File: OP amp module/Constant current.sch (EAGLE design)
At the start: 6 parts, among them IC1 LM358N

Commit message: Constant current
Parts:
- removed R3: 1M, rcl:R-US_0414/15
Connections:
- removed net N$1: IC1A.+IN, IC2.OUT, R1.1
- removed net N$5: IC1A.-IN, R2.2, VR1.E, VR1.S
- new net N$2: IC1A.OUT, IC2.ADJ, VR1.A, VR1.S
- new net N$4: IC2.OUT, R1.1, R2.2
- net GND: no longer R3.2
- net N$3: now also IC1A.-IN, R2.1, VR1.E; no longer IC1A.OUT, IC2.ADJ, VR1.A
- net N$6: now also IC1A.+IN; no longer R2.1, R3.1
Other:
- moved on the sheet: IC1A, R1, R2, VR1
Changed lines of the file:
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@@
 <part name="VR1" library="My Library" deviceset="POT" device="100K_3362U" value="5k"/>
 <part name="R2" library="rcl" deviceset="R-US_" device="0414/15" value="1k"/>
-<part name="R3" library="rcl" deviceset="R-US_" device="0414/15" value="1M"/>
 </parts>
 <sheets>
@@
 </plain>
 <instances>
-<instance part="IC1" gate="A" x="40.64" y="55.88" rot="MR0"/>
+<instance part="IC1" gate="A" x="35.56" y="45.72" rot="R180"/>
 <instance part="IC2" gate="1" x="27.94" y="73.66"/>
-<instance part="R1" gate="G$1" x="58.42" y="73.66"/>
+<instance part="R1" gate="G$1" x="63.5" y="63.5" rot="R270"/>
 <instance part="P+1" gate="1" x="12.7" y="78.74"/>
-<instance part="IC1" gate="P" x="40.64" y="55.88"/>
-<instance part="P+2" gate="1" x="40.64" y="66.04"/>
-<instance part="GND1" gate="1" x="40.64" y="30.48"/>
-<instance part="GND2" gate="1" x="71.12" y="30.48"/>
-<instance part="GND3" gate="1" x="12.7" y="30.48"/>
-<instance part="VR1" gate="G$1" x="48.26" y="45.72" rot="R270"/>
-<instance part="R2" gate="G$1" x="60.96" y="53.34" rot="R180"/>
-<instance part="R3" gate="G$1" x="66.04" y="43.18" rot="R270"/>
+<instance part="IC1" gate="P" x="35.56" y="45.72"/>
+<instance part="P+2" gate="1" x="35.56" y="55.88"/>
+<instance part="GND1" gate="1" x="35.56" y="27.94"/>
+<instance part="GND2" gate="1" x="63.5" y="27.94"/>
+<instance part="GND3" gate="1" x="7.62" y="27.94"/>
+<instance part="VR1" gate="G$1" x="45.72" y="63.5" rot="R270"/>
+<instance part="R2" gate="G$1" x="53.34" y="68.58" rot="R90"/>
 </instances>
 <busses>
 </busses>
 <nets>
-<net name="N$1" class="0">
-<segment>
-<pinref part="IC2" gate="1" pin="OUT"/>
-<pinref part="R1" gate="G$1" pin="1"/>
-<wire x1="38.1" y1="73.66" x2="53.34" y2="73.66" width="0.1524" layer="91"/>
-<wire x1="53.34" y1="73.66" x2="53.34" y2="58.42" width="0.1524" layer="91"/>
-<pinref part="IC1" gate="A" pin="+IN"/>
-<wire x1="53.34" y1="58.42" x2="48.26" y2="58.42" width="0.1524" layer="91"/>
-<junction x="53.34" y="73.66"/>
-</segment>
-</net>
-<net name="N$3" class="0">
-<segment>
-<pinref part="IC2" gate="1" pin="ADJ"/>
-<wire x1="27.94" y1="66.04" x2="27.94" y2="55.88" width="0.1524" layer="91"/>
-<pinref part="IC1" gate="A" pin="OUT"/>
-<wire x1="27.94" y1="55.88" x2="33.02" y2="55.88" width="0.1524" layer="91"/>
-<wire x1="43.18" y1="45.72" x2="27.94" y2="45.72" width="0.1524" layer="91"/>
-<wire x1="27.94" y1="45.72" x2="27.94" y2="55.88" width="0.1524" layer="91"/>
-<junction x="27.94" y="55.88"/>
-<pinref part="VR1" gate="G$1" pin="A"/>
-</segment>
-</net>
 <net name="VCC" class="0">
 <segment>
@@
 <pinref part="P+2" gate="1" pin="VCC"/>
 <pinref part="IC1" gate="P" pin="V+"/>
-<wire x1="40.64" y1="66.04" x2="40.64" y2="63.5" width="0.1524" layer="91"/>
+<wire x1="35.56" y1="55.88" x2="35.56" y2="53.34" width="0.1524" layer="91"/>
 </segment>
 </net>
@@
 <pinref part="IC1" gate="P" pin="V-"/>
 <pinref part="GND1" gate="1" pin="GND"/>
-<wire x1="40.64" y1="48.26" x2="40.64" y2="33.02" width="0.1524" layer="91"/>
+<wire x1="35.56" y1="38.1" x2="35.56" y2="30.48" width="0.1524" layer="91"/>
 </segment>
 <segment>
-<wire x1="81.28" y1="35.56" x2="71.12" y2="35.56" width="0.1524" layer="91"/>
+<wire x1="68.58" y1="33.02" x2="63.5" y2="33.02" width="0.1524" layer="91"/>
 <pinref part="GND2" gate="1" pin="GND"/>
-<wire x1="71.12" y1="35.56" x2="71.12" y2="33.02" width="0.1524" layer="91"/>
-<pinref part="R3" gate="G$1" pin="2"/>
-<wire x1="71.12" y1="35.56" x2="66.04" y2="35.56" width="0.1524" layer="91"/>
-<wire x1="66.04" y1="35.56" x2="66.04" y2="38.1" width="0.1524" layer="91"/>
+<wire x1="63.5" y1="33.02" x2="63.5" y2="30.48" width="0.1524" layer="91"/>
 </segment>
 <segment>
 <pinref part="GND3" gate="1" pin="GND"/>
-<wire x1="12.7" y1="33.02" x2="12.7" y2="45.72" width="0.1524" layer="91"/>
-<wire x1="12.7" y1="45.72" x2="5.08" y2="45.72" width="0.1524" layer="91"/>
+<wire x1="7.62" y1="30.48" x2="7.62" y2="40.64" width="0.1524" layer="91"/>
+<wire x1="7.62" y1="40.64" x2="5.08" y2="40.64" width="0.1524" layer="91"/>
 </segment>
 </net>
 <net name="N$6" class="0">
 <segment>
-<pinref part="R2" gate="G$1" pin="1"/>
 <pinref part="R1" gate="G$1" pin="2"/>
-<wire x1="63.5" y1="73.66" x2="66.04" y2="73.66" width="0.1524" layer="91"/>
-<wire x1="66.04" y1="73.66" x2="81.28" y2="73.66" width="0.1524" layer="91"/>
-<wire x1="66.04" y1="53.34" x2="66.04" y2="73.66" width="0.1524" layer="91"/>
-<junction x="66.04" y="73.66"/>
-<pinref part="R3" gate="G$1" pin="1"/>
-<wire x1="66.04" y1="48.26" x2="66.04" y2="53.34" width="0.1524" layer="91"/>
-<junction x="66.04" y="53.34"/>
+<wire x1="63.5" y1="58.42" x2="63.5" y2="43.18" width="0.1524" layer="91"/>
+<pinref part="IC1" gate="A" pin="+IN"/>
+<wire x1="63.5" y1="43.18" x2="68.58" y2="43.18" width="0.1524" layer="91"/>
+<wire x1="43.18" y1="43.18" x2="63.5" y2="43.18" width="0.1524" layer="91"/>
+<junction x="63.5" y="43.18"/>
 </segment>
 </net>
-<net name="N$5" class="0">
+<net name="N$2" class="0">
 <segment>
-<wire x1="55.88" y1="45.72" x2="53.34" y2="45.72" width="0.1524" layer="91"/>
-<pinref part="IC1" gate="A" pin="-IN"/>
-<pinref part="R2" gate="G$1" pin="2"/>
-<wire x1="48.26" y1="53.34" x2="55.88" y2="53.34" width="0.1524" layer="91"/>
-<wire x1="55.88" y1="45.72" x2="55.88" y2="53.34" width="0.1524" layer="91"/>
-<junction x="55.88" y="53.34"/>
+<pinref part="IC1" gate="A" pin="OUT"/>
+<wire x1="27.94" y1="45.72" x2="27.94" y2="63.5" width="0.1524" layer="91"/>
+<pinref part="VR1" gate="G$1" pin="A"/>
+<wire x1="27.94" y1="63.5" x2="40.64" y2="63.5" width="0.1524" layer="91"/>
+<pinref part="IC2" gate="1" pin="ADJ"/>
+<wire x1="27.94" y1="66.04" x2="27.94" y2="63.5" width="0.1524" layer="91"/>
+<wire x1="27.94" y1="63.5" x2="27.94" y2="58.42" width="0.1524" layer="91"/>
+<wire x1="27.94" y1="58.42" x2="27.94" y2="63.5" width="0.1524" layer="91"/>
 <pinref part="VR1" gate="G$1" pin="S"/>
-<wire x1="48.26" y1="40.64" x2="53.34" y2="40.64" width="0.1524" layer="91"/>
-<wire x1="53.34" y1="40.64" x2="53.34" y2="45.72" width="0.1524" layer="91"/>
-<pinref part="VR1" gate="G$1" pin="E"/>
-<junction x="53.34" y="45.72"/>
+<wire x1="45.72" y1="58.42" x2="40.64" y2="58.42" width="0.1524" layer="91"/>
+<wire x1="40.64" y1="58.42" x2="40.64" y2="63.5" width="0.1524" layer="91"/>
+<junction x="27.94" y="63.5"/>
+<junction x="40.64" y="63.5"/>
 </segment>
 </net>
+<net name="N$3" class="0">
+<segment>
+<pinref part="VR1" gate="G$1" pin="E"/>
+<pinref part="R2" gate="G$1" pin="1"/>
+<wire x1="50.8" y1="63.5" x2="53.34" y2="63.5" width="0.1524" layer="91"/>
+<wire x1="53.34" y1="63.5" x2="53.34" y2="48.26" width="0.1524" layer="91"/>
+<pinref part="IC1" gate="A" pin="-IN"/>
+<wire x1="53.34" y1="48.26" x2="43.18" y2="48.26" width="0.1524" layer="91"/>
+<junction x="53.34" y="63.5"/>
+</segment>
+</net>
+<net name="N$4" class="0">
+<segment>
+<pinref part="IC2" gate="1" pin="OUT"/>
+<pinref part="R2" gate="G$1" pin="2"/>
+<wire x1="38.1" y1="73.66" x2="53.34" y2="73.66" width="0.1524" layer="91"/>
+<wire x1="53.34" y1="73.66" x2="63.5" y2="73.66" width="0.1524" layer="91"/>
+<wire x1="63.5" y1="73.66" x2="63.5" y2="68.58" width="0.1524" layer="91"/>
+<junction x="53.34" y="73.66"/>
+<pinref part="R1" gate="G$1" pin="1"/>
+</segment>
+</net>

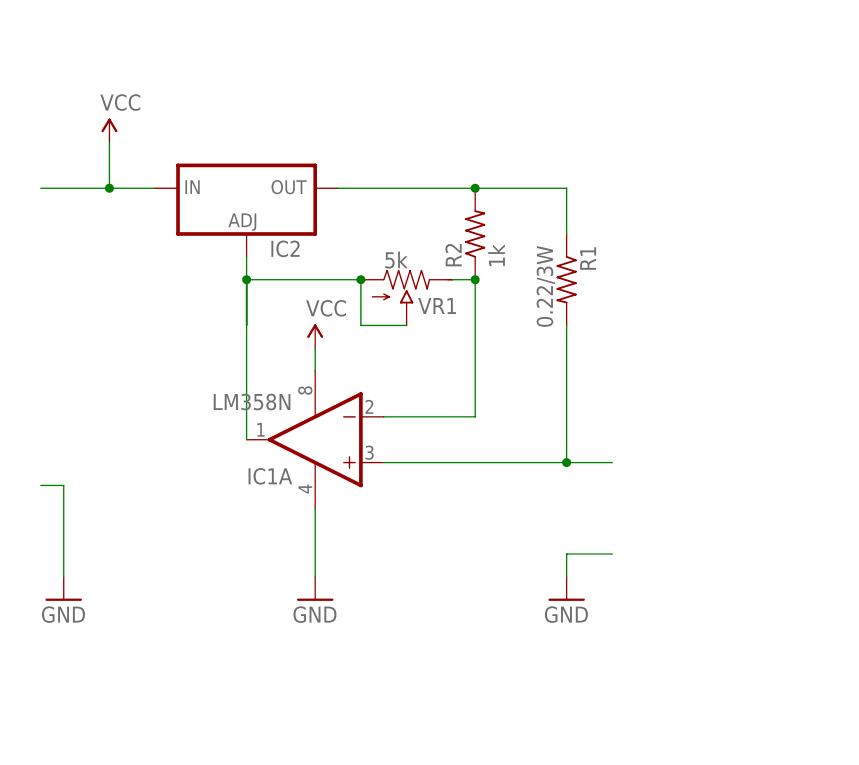
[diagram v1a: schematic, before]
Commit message: const. current
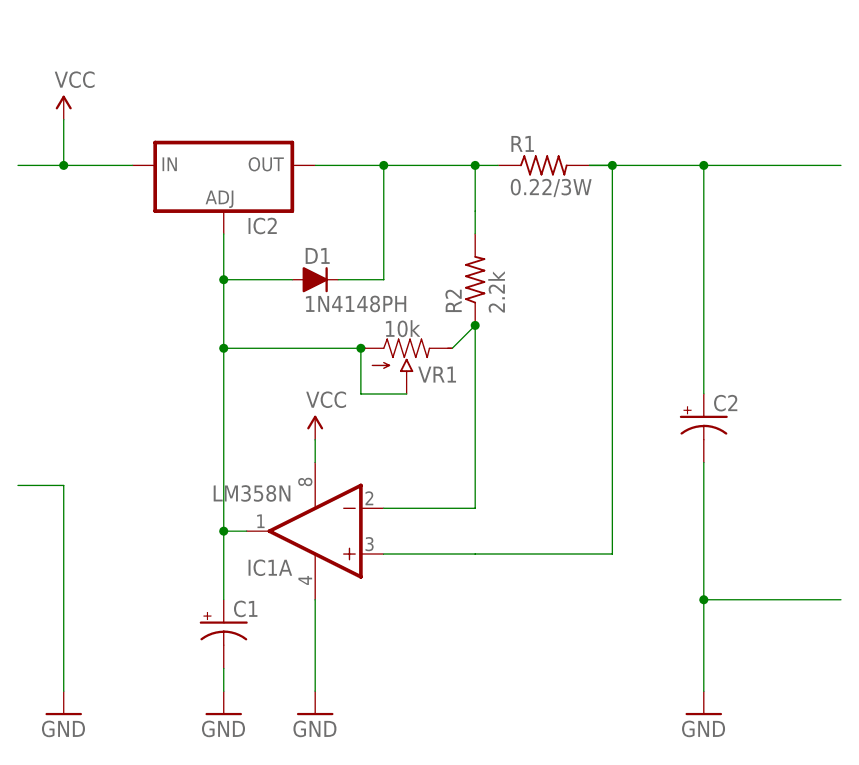
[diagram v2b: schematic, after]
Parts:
- added C1, C2: (no value), SparkFun:CAP_POLPTH1
- added D1: 1N4148PH, JPN:1N4148PH
- R2: value 1k -> 2.2k
- VR1: value 5k -> 10k
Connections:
- removed net N$4: IC2.OUT, R1.1, R2.2
- new net N$1: D1.C, IC2.OUT, R1.1, R2.2
- net GND: now also C1.-, C2.-
- net N$2: now also C1.+, D1.A
- net N$6: now also C2.+
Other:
- moved on the sheet: IC1A, IC2, R1, R2, VR1
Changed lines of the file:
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@@
 <part name="GND2" library="SparkFun" deviceset="GND" device=""/>
 <part name="GND3" library="SparkFun" deviceset="GND" device=""/>
-<part name="VR1" library="My Library" deviceset="POT" device="100K_3362U" value="5k"/>
-<part name="R2" library="rcl" deviceset="R-US_" device="0414/15" value="1k"/>
+<part name="VR1" library="My Library" deviceset="POT" device="100K_3362U" value="10k"/>
+<part name="R2" library="rcl" deviceset="R-US_" device="0414/15" value="2.2k"/>
+<part name="C1" library="SparkFun" deviceset="CAP_POL" device="PTH1"/>
+<part name="GND4" library="SparkFun" deviceset="GND" device=""/>
+<part name="D1" library="JPN" deviceset="1N4148" device="PH"/>
+<part name="C2" library="SparkFun" deviceset="CAP_POL" device="PTH1"/>
 </parts>
 <sheets>
@@
 </plain>
 <instances>
-<instance part="IC1" gate="A" x="35.56" y="45.72" rot="R180"/>
-<instance part="IC2" gate="1" x="27.94" y="73.66"/>
-<instance part="R1" gate="G$1" x="63.5" y="63.5" rot="R270"/>
-<instance part="P+1" gate="1" x="12.7" y="78.74"/>
-<instance part="IC1" gate="P" x="35.56" y="45.72"/>
-<instance part="P+2" gate="1" x="35.56" y="55.88"/>
-<instance part="GND1" gate="1" x="35.56" y="27.94"/>
-<instance part="GND2" gate="1" x="63.5" y="27.94"/>
-<instance part="GND3" gate="1" x="7.62" y="27.94"/>
-<instance part="VR1" gate="G$1" x="45.72" y="63.5" rot="R270"/>
-<instance part="R2" gate="G$1" x="53.34" y="68.58" rot="R90"/>
+<instance part="IC1" gate="A" x="35.56" y="35.56" rot="R180"/>
+<instance part="IC2" gate="1" x="25.4" y="76.2"/>
+<instance part="R1" gate="G$1" x="60.96" y="76.2"/>
+<instance part="P+1" gate="1" x="7.62" y="81.28"/>
+<instance part="IC1" gate="P" x="35.56" y="35.56"/>
+<instance part="P+2" gate="1" x="35.56" y="45.72"/>
+<instance part="GND1" gate="1" x="35.56" y="15.24"/>
+<instance part="GND2" gate="1" x="78.74" y="15.24"/>
+<instance part="GND3" gate="1" x="7.62" y="15.24"/>
+<instance part="VR1" gate="G$1" x="45.72" y="55.88" rot="R270"/>
+<instance part="R2" gate="G$1" x="53.34" y="63.5" rot="R90"/>
+<instance part="C1" gate="G$1" x="25.4" y="25.4"/>
+<instance part="GND4" gate="1" x="25.4" y="15.24"/>
+<instance part="D1" gate="G$1" x="35.56" y="63.5"/>
+<instance part="C2" gate="G$1" x="78.74" y="48.26"/>
 </instances>
 <busses>
@@
 <segment>
 <pinref part="IC2" gate="1" pin="IN"/>
-<wire x1="17.78" y1="73.66" x2="12.7" y2="73.66" width="0.1524" layer="91"/>
 <pinref part="P+1" gate="1" pin="VCC"/>
-<wire x1="12.7" y1="73.66" x2="5.08" y2="73.66" width="0.1524" layer="91"/>
-<wire x1="12.7" y1="73.66" x2="12.7" y2="78.74" width="0.1524" layer="91"/>
-<junction x="12.7" y="73.66"/>
+<wire x1="15.24" y1="76.2" x2="7.62" y2="76.2" width="0.1524" layer="91"/>
+<wire x1="7.62" y1="76.2" x2="2.54" y2="76.2" width="0.1524" layer="91"/>
+<wire x1="7.62" y1="76.2" x2="7.62" y2="81.28" width="0.1524" layer="91"/>
+<junction x="7.62" y="76.2"/>
 </segment>
 <segment>
 <pinref part="P+2" gate="1" pin="VCC"/>
 <pinref part="IC1" gate="P" pin="V+"/>
-<wire x1="35.56" y1="55.88" x2="35.56" y2="53.34" width="0.1524" layer="91"/>
+<wire x1="35.56" y1="45.72" x2="35.56" y2="43.18" width="0.1524" layer="91"/>
 </segment>
 </net>
@@
 <pinref part="IC1" gate="P" pin="V-"/>
 <pinref part="GND1" gate="1" pin="GND"/>
-<wire x1="35.56" y1="38.1" x2="35.56" y2="30.48" width="0.1524" layer="91"/>
+<wire x1="35.56" y1="27.94" x2="35.56" y2="17.78" width="0.1524" layer="91"/>
 </segment>
 <segment>
-<wire x1="68.58" y1="33.02" x2="63.5" y2="33.02" width="0.1524" layer="91"/>
+<wire x1="93.98" y1="27.94" x2="78.74" y2="27.94" width="0.1524" layer="91"/>
 <pinref part="GND2" gate="1" pin="GND"/>
-<wire x1="63.5" y1="33.02" x2="63.5" y2="30.48" width="0.1524" layer="91"/>
+<wire x1="78.74" y1="27.94" x2="78.74" y2="17.78" width="0.1524" layer="91"/>
+<pinref part="C2" gate="G$1" pin="-"/>
+<wire x1="78.74" y1="43.18" x2="78.74" y2="27.94" width="0.1524" layer="91"/>
+<junction x="78.74" y="27.94"/>
 </segment>
 <segment>
 <pinref part="GND3" gate="1" pin="GND"/>
-<wire x1="7.62" y1="30.48" x2="7.62" y2="40.64" width="0.1524" layer="91"/>
-<wire x1="7.62" y1="40.64" x2="5.08" y2="40.64" width="0.1524" layer="91"/>
+<wire x1="7.62" y1="17.78" x2="7.62" y2="40.64" width="0.1524" layer="91"/>
+<wire x1="7.62" y1="40.64" x2="2.54" y2="40.64" width="0.1524" layer="91"/>
+</segment>
+<segment>
+<pinref part="C1" gate="G$1" pin="-"/>
+<wire x1="25.4" y1="20.32" x2="25.4" y2="17.78" width="0.1524" layer="91"/>
+<pinref part="GND4" gate="1" pin="GND"/>
 </segment>
 </net>
@@
 <segment>
 <pinref part="R1" gate="G$1" pin="2"/>
-<wire x1="63.5" y1="58.42" x2="63.5" y2="43.18" width="0.1524" layer="91"/>
+<wire x1="66.04" y1="76.2" x2="68.58" y2="76.2" width="0.1524" layer="91"/>
+<wire x1="68.58" y1="76.2" x2="68.58" y2="33.02" width="0.1524" layer="91"/>
 <pinref part="IC1" gate="A" pin="+IN"/>
-<wire x1="63.5" y1="43.18" x2="68.58" y2="43.18" width="0.1524" layer="91"/>
-<wire x1="43.18" y1="43.18" x2="63.5" y2="43.18" width="0.1524" layer="91"/>
-<junction x="63.5" y="43.18"/>
+<wire x1="43.18" y1="33.02" x2="53.34" y2="33.02" width="0.1524" layer="91"/>
+<wire x1="53.34" y1="33.02" x2="68.58" y2="33.02" width="0.1524" layer="91"/>
+<wire x1="66.04" y1="76.2" x2="68.58" y2="76.2" width="0.1524" layer="91"/>
+<junction x="68.58" y="76.2"/>
+<wire x1="68.58" y1="76.2" x2="78.74" y2="76.2" width="0.1524" layer="91"/>
+<pinref part="C2" gate="G$1" pin="+"/>
+<wire x1="78.74" y1="76.2" x2="93.98" y2="76.2" width="0.1524" layer="91"/>
+<wire x1="78.74" y1="50.8" x2="78.74" y2="76.2" width="0.1524" layer="91"/>
+<junction x="78.74" y="76.2"/>
 </segment>
 </net>
@@
 <segment>
 <pinref part="IC1" gate="A" pin="OUT"/>
-<wire x1="27.94" y1="45.72" x2="27.94" y2="63.5" width="0.1524" layer="91"/>
+<wire x1="27.94" y1="35.56" x2="25.4" y2="35.56" width="0.1524" layer="91"/>
 <pinref part="VR1" gate="G$1" pin="A"/>
-<wire x1="27.94" y1="63.5" x2="40.64" y2="63.5" width="0.1524" layer="91"/>
+<wire x1="25.4" y1="35.56" x2="25.4" y2="55.88" width="0.1524" layer="91"/>
+<wire x1="25.4" y1="55.88" x2="40.64" y2="55.88" width="0.1524" layer="91"/>
 <pinref part="IC2" gate="1" pin="ADJ"/>
-<wire x1="27.94" y1="66.04" x2="27.94" y2="63.5" width="0.1524" layer="91"/>
-<wire x1="27.94" y1="63.5" x2="27.94" y2="58.42" width="0.1524" layer="91"/>
-<wire x1="27.94" y1="58.42" x2="27.94" y2="63.5" width="0.1524" layer="91"/>
+<wire x1="25.4" y1="68.58" x2="25.4" y2="63.5" width="0.1524" layer="91"/>
 <pinref part="VR1" gate="G$1" pin="S"/>
-<wire x1="45.72" y1="58.42" x2="40.64" y2="58.42" width="0.1524" layer="91"/>
-<wire x1="40.64" y1="58.42" x2="40.64" y2="63.5" width="0.1524" layer="91"/>
-<junction x="27.94" y="63.5"/>
-<junction x="40.64" y="63.5"/>
+<wire x1="25.4" y1="63.5" x2="25.4" y2="55.88" width="0.1524" layer="91"/>
+<wire x1="45.72" y1="50.8" x2="40.64" y2="50.8" width="0.1524" layer="91"/>
+<wire x1="40.64" y1="50.8" x2="40.64" y2="55.88" width="0.1524" layer="91"/>
+<junction x="25.4" y="55.88"/>
+<junction x="40.64" y="55.88"/>
+<pinref part="C1" gate="G$1" pin="+"/>
+<wire x1="25.4" y1="27.94" x2="25.4" y2="35.56" width="0.1524" layer="91"/>
+<junction x="25.4" y="35.56"/>
+<pinref part="D1" gate="G$1" pin="A"/>
+<wire x1="33.02" y1="63.5" x2="25.4" y2="63.5" width="0.1524" layer="91"/>
+<junction x="25.4" y="63.5"/>
 </segment>
 </net>
@@
 <pinref part="VR1" gate="G$1" pin="E"/>
 <pinref part="R2" gate="G$1" pin="1"/>
-<wire x1="50.8" y1="63.5" x2="53.34" y2="63.5" width="0.1524" layer="91"/>
-<wire x1="53.34" y1="63.5" x2="53.34" y2="48.26" width="0.1524" layer="91"/>
+<wire x1="50.8" y1="55.88" x2="53.34" y2="58.42" width="0.1524" layer="91"/>
+<wire x1="53.34" y1="58.42" x2="53.34" y2="38.1" width="0.1524" layer="91"/>
 <pinref part="IC1" gate="A" pin="-IN"/>
-<wire x1="53.34" y1="48.26" x2="43.18" y2="48.26" width="0.1524" layer="91"/>
-<junction x="53.34" y="63.5"/>
+<wire x1="53.34" y1="38.1" x2="43.18" y2="38.1" width="0.1524" layer="91"/>
+<junction x="53.34" y="58.42"/>
 </segment>
 </net>
-<net name="N$4" class="0">
+<net name="N$1" class="0">
 <segment>
 <pinref part="IC2" gate="1" pin="OUT"/>
+<pinref part="R1" gate="G$1" pin="1"/>
+<wire x1="35.56" y1="76.2" x2="43.18" y2="76.2" width="0.1524" layer="91"/>
 <pinref part="R2" gate="G$1" pin="2"/>
-<wire x1="38.1" y1="73.66" x2="53.34" y2="73.66" width="0.1524" layer="91"/>
-<wire x1="53.34" y1="73.66" x2="63.5" y2="73.66" width="0.1524" layer="91"/>
-<wire x1="63.5" y1="73.66" x2="63.5" y2="68.58" width="0.1524" layer="91"/>
-<junction x="53.34" y="73.66"/>
-<pinref part="R1" gate="G$1" pin="1"/>
+<wire x1="43.18" y1="76.2" x2="53.34" y2="76.2" width="0.1524" layer="91"/>
+<wire x1="53.34" y1="76.2" x2="55.88" y2="76.2" width="0.1524" layer="91"/>
+<wire x1="53.34" y1="68.58" x2="53.34" y2="71.12" width="0.1524" layer="91"/>
+<wire x1="53.34" y1="71.12" x2="53.34" y2="76.2" width="0.1524" layer="91"/>
+<junction x="53.34" y="76.2"/>
+<pinref part="D1" gate="G$1" pin="C"/>
+<wire x1="38.1" y1="63.5" x2="43.18" y2="63.5" width="0.1524" layer="91"/>
+<wire x1="43.18" y1="63.5" x2="43.18" y2="76.2" width="0.1524" layer="91"/>
+<junction x="43.18" y="76.2"/>
 </segment>
 </net>

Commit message: My Library
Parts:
- added R3: 10k, SparkFun:RESISTORKIT
- R2: value 2.2k -> 10k
- VR1: value 10k -> 100k
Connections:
- new net N$4: R3.2, VR1.A, VR1.S
- net N$2: now also R3.1; no longer VR1.A, VR1.S
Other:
- moved on the sheet: C1, C2, D1, IC1A, R1, R2, VR1
